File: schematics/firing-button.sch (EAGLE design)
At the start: 1 part

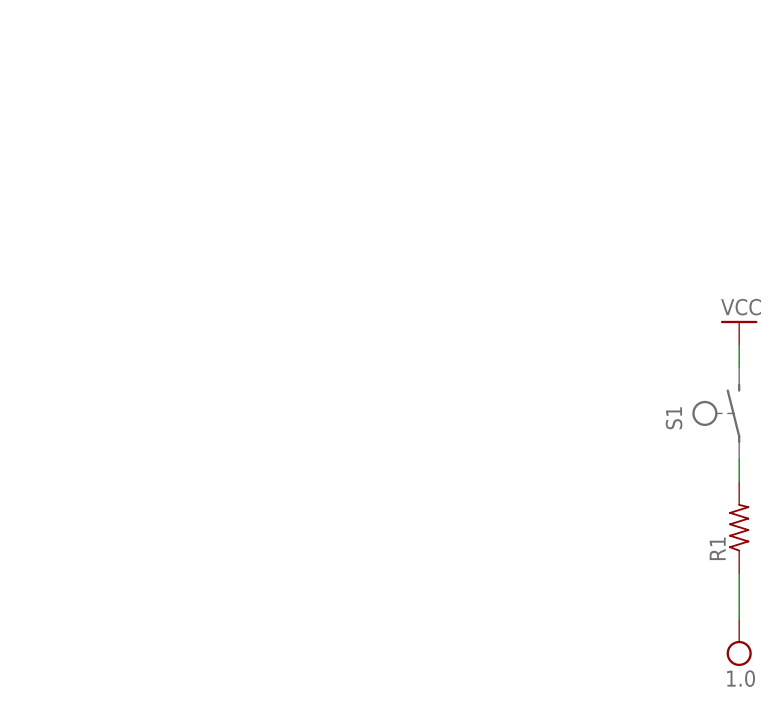
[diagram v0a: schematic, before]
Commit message: Updated schematics to have appropriate pins and to fit most recent updates.  Final report updated and ready for review.
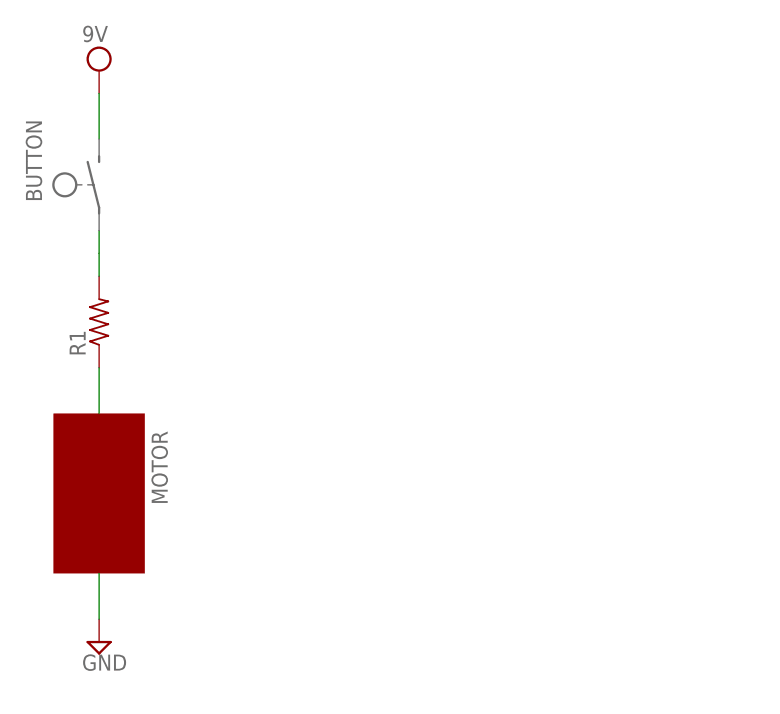
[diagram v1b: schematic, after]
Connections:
- net VCC renamed N$24
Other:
- note added: "MOTOR"
- moved on the sheet: R1
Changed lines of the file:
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@@
 <layer number="48" name="Document" color="7" fill="1" visible="no" active="no"/>
 <layer number="49" name="Reference" color="7" fill="1" visible="no" active="no"/>
-<layer number="51" name="tDocu" color="6" fill="1" visible="no" active="no"/>
+<layer number="50" name="dxf" color="7" fill="1" visible="no" active="no"/>
+<layer number="51" name="tDocu" color="7" fill="1" visible="no" active="no"/>
 <layer number="52" name="bDocu" color="7" fill="1" visible="no" active="no"/>
 <layer number="90" name="Modules" color="5" fill="1" visible="yes" active="yes"/>
@@
 <layer number="97" name="Info" color="7" fill="1" visible="yes" active="yes"/>
 <layer number="98" name="Guide" color="6" fill="1" visible="yes" active="yes"/>
+<layer number="99" name="SpiceOrder" color="5" fill="1" visible="yes" active="yes"/>
+<layer number="100" name="Muster" color="7" fill="1" visible="yes" active="yes"/>
+<layer number="101" name="Flex-Kleb" color="1" fill="7" visible="yes" active="yes"/>
+<layer number="102" name="fp2" color="7" fill="1" visible="yes" active="yes"/>
+<layer number="103" name="fp3" color="7" fill="1" visible="yes" active="yes"/>
+<layer number="104" name="fp4" color="7" fill="1" visible="yes" active="yes"/>
+<layer number="105" name="Beschreib" color="9" fill="1" visible="yes" active="yes"/>
+<layer number="106" name="BGA-Top" color="4" fill="1" visible="yes" active="yes"/>
+<layer number="107" name="BD-Top" color="5" fill="1" visible="yes" active="yes"/>
+<layer number="108" name="fp8" color="7" fill="1" visible="yes" active="yes"/>
+<layer number="109" name="fp9" color="7" fill="1" visible="yes" active="yes"/>
+<layer number="110" name="fp0" color="7" fill="1" visible="yes" active="yes"/>
+<layer number="116" name="Patch_BOT" color="9" fill="4" visible="yes" active="yes"/>
+<layer number="121" name="tTestdril" color="7" fill="1" visible="yes" active="yes"/>
+<layer number="122" name="bTestdril" color="7" fill="1" visible="yes" active="yes"/>
+<layer number="123" name="tTestmark" color="7" fill="1" visible="yes" active="yes"/>
+<layer number="124" name="bTestmark" color="7" fill="1" visible="yes" active="yes"/>
+<layer number="131" name="tAdjust" color="7" fill="1" visible="yes" active="yes"/>
+<layer number="132" name="bAdjust" color="7" fill="1" visible="yes" active="yes"/>
+<layer number="200" name="200bmp" color="7" fill="1" visible="yes" active="yes"/>
+<layer number="201" name="201bmp" color="7" fill="1" visible="yes" active="yes"/>
+<layer number="202" name="202bmp" color="7" fill="1" visible="yes" active="yes"/>
+<layer number="203" name="203bmp" color="7" fill="1" visible="yes" active="yes"/>
+<layer number="204" name="204bmp" color="7" fill="1" visible="yes" active="yes"/>
+<layer number="205" name="205bmp" color="7" fill="1" visible="yes" active="yes"/>
+<layer number="206" name="206bmp" color="7" fill="1" visible="yes" active="yes"/>
+<layer number="207" name="207bmp" color="7" fill="1" visible="yes" active="yes"/>
+<layer number="208" name="208bmp" color="7" fill="1" visible="yes" active="yes"/>
+<layer number="209" name="209bmp" color="7" fill="1" visible="yes" active="yes"/>
+<layer number="210" name="210bmp" color="7" fill="1" visible="yes" active="yes"/>
+<layer number="250" name="Descript" color="3" fill="1" visible="no" active="no"/>
+<layer number="251" name="SMDround" color="12" fill="11" visible="no" active="no"/>
+<layer number="254" name="OrgLBR" color="7" fill="1" visible="yes" active="yes"/>
 </layers>
 <schematic xreflabel="%F%N/%S.%C%R" xrefpart="/%S.%C%R">
@@
 <parts>
 <part name="R1" library="rcl" deviceset="R-US_" device="0204/2V"/>
-<part name="SUPPLY1" library="supply2" deviceset="VCC" device="" value="1.0"/>
-<part name="GND1" library="supply1" deviceset="GND" device="" value="VCC"/>
-<part name="S1" library="switch-omron" deviceset="D-GS" device=""/>
+<part name="SUPPLY14" library="supply2" deviceset="GND" device=""/>
+<part name="BUTTON" library="switch-omron" deviceset="D-GS" device=""/>
+<part name="SUPPLY1" library="supply2" deviceset="VCC" device="" value="9V"/>
 </parts>
 <sheets>
 <sheet>
 <plain>
+<text x="15.24" y="48.26" size="1.778" layer="95" rot="R90">MOTOR</text>
+<rectangle x1="-1.27" y1="44.45" x2="16.51" y2="54.61" layer="94" rot="R90"/>
 </plain>
 <instances>
-<instance part="R1" gate="G$1" x="78.74" y="45.72" rot="R90"/>
-<instance part="SUPPLY1" gate="G$1" x="78.74" y="33.02" rot="R180"/>
-<instance part="GND1" gate="1" x="78.74" y="68.58" rot="R180"/>
-<instance part="S1" gate="G$1" x="78.74" y="58.42"/>
+<instance part="R1" gate="G$1" x="7.62" y="68.58" rot="R90"/>
+<instance part="SUPPLY14" gate="GND" x="7.62" y="33.02"/>
+<instance part="BUTTON" gate="G$1" x="7.62" y="83.82"/>
+<instance part="SUPPLY1" gate="G$1" x="7.62" y="96.52"/>
 </instances>
 <busses>
 </busses>
 <nets>
-<net name="VCC" class="0">
+<net name="N$24" class="0">
 <segment>
 <pinref part="R1" gate="G$1" pin="1"/>
-<pinref part="SUPPLY1" gate="G$1" pin="VCC"/>
-<wire x1="78.74" y1="40.64" x2="78.74" y2="35.56" width="0.1524" layer="91"/>
+<wire x1="7.62" y1="63.5" x2="7.62" y2="58.42" width="0.1524" layer="91"/>
 </segment>
 </net>
@@
 <segment>
 <pinref part="R1" gate="G$1" pin="2"/>
-<wire x1="78.74" y1="53.34" x2="78.74" y2="50.8" width="0.1524" layer="91"/>
+<wire x1="7.62" y1="73.66" x2="7.62" y2="76.2" width="0.1524" layer="91"/>
+</segment>
+</net>
+<net name="N$3" class="0">
+<segment>
+<wire x1="7.62" y1="76.2" x2="7.62" y2="78.74" width="0.1524" layer="91"/>
 </segment>
 </net>
 <net name="GND" class="0">
 <segment>
-<pinref part="GND1" gate="1" pin="GND"/>
-<wire x1="78.74" y1="63.5" x2="78.74" y2="66.04" width="0.1524" layer="91"/>
+<pinref part="SUPPLY14" gate="GND" pin="GND"/>
+<wire x1="7.62" y1="35.56" x2="7.62" y2="40.64" width="0.1524" layer="91"/>
 </segment>
 </net>
+<net name="VCC" class="0">
+<segment>
+<pinref part="SUPPLY1" gate="G$1" pin="VCC"/>
+<wire x1="7.62" y1="88.9" x2="7.62" y2="93.98" width="0.1524" layer="91"/>
+</segment>
+</net>
